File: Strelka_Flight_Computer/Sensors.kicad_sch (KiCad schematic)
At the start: 5 parts

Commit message: Started design for V2
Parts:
- added TP11, TP2, TP5: TestPoint, TestPoint:TestPoint_Pad_1.0x1.0mm, symbol Connector:TestPoint
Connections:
- net CS_ACCEL: now also TP2.1
- net CS_GYRO: now also TP5.1
- net CS_MAG: now also TP11.1
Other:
- note added: "Good Gyro Options - 511-I3G4250DTR - 410-IAM-20380 - ASM330LHHXTR"
- moved on the sheet: TP6, TP7, TP8

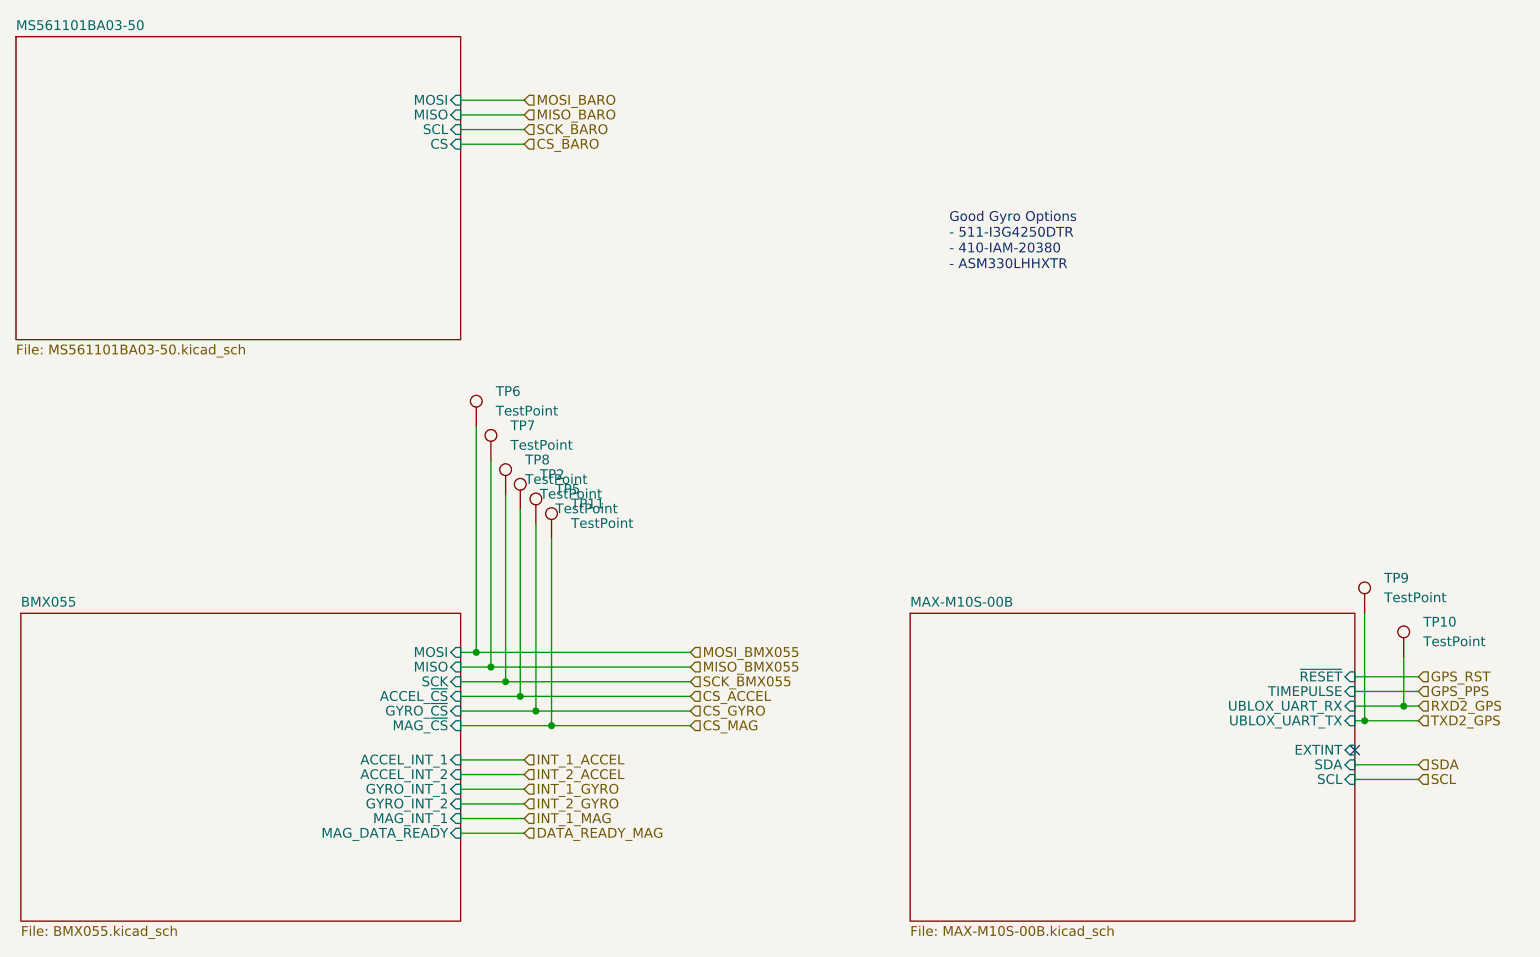
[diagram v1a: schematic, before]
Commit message: Changes main processor to h4745
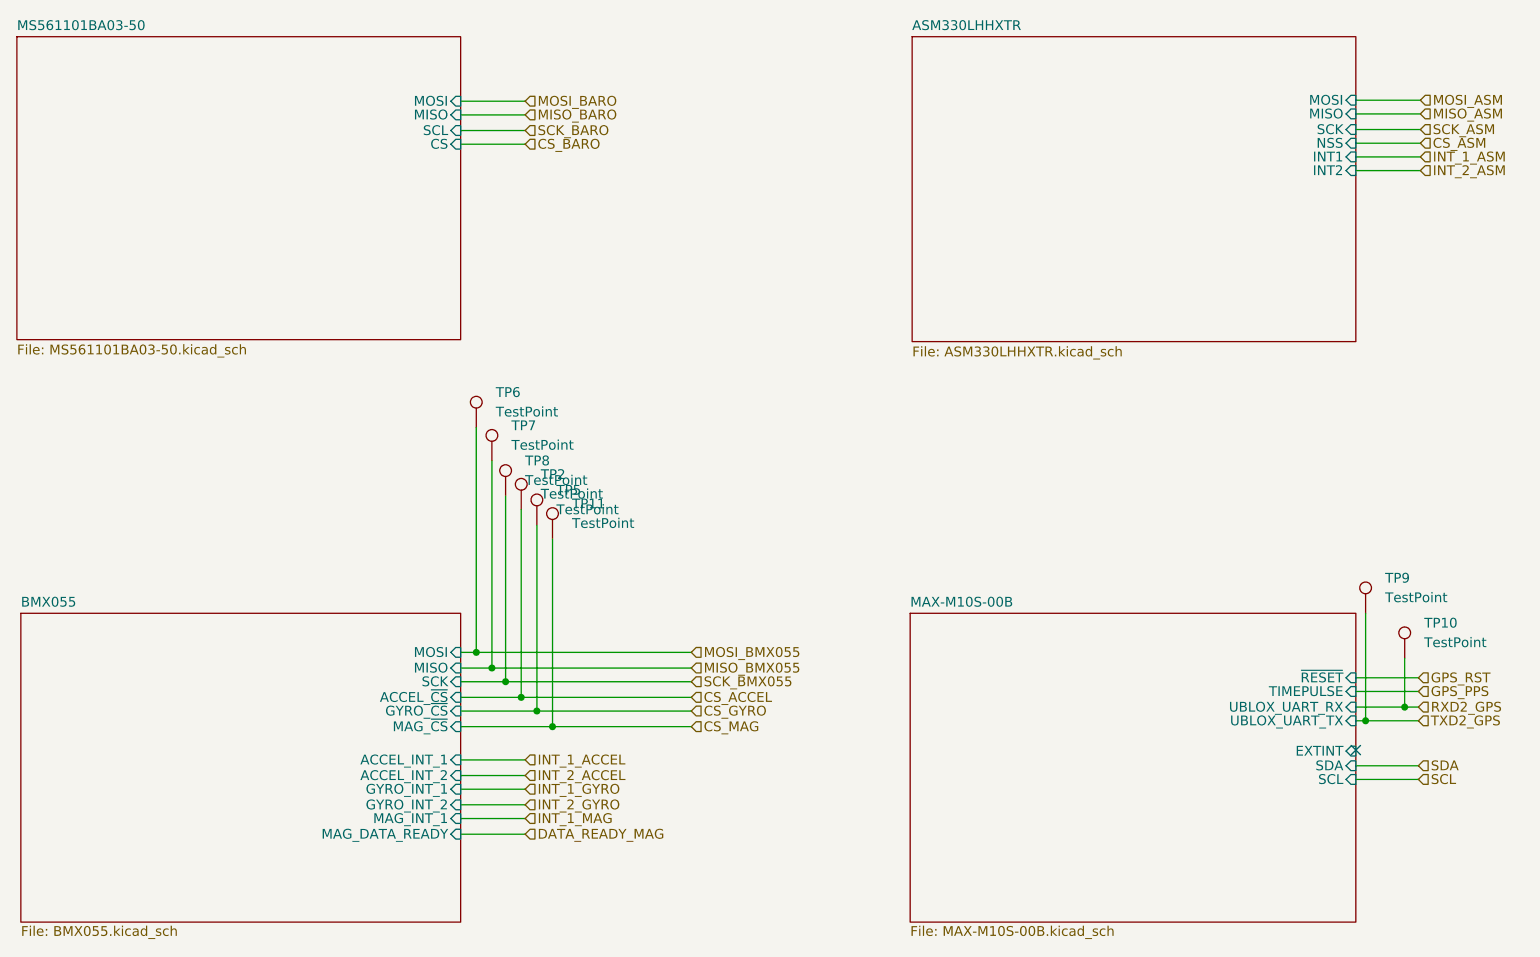
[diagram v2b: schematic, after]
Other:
- added sheet ASM330LHHXTR (ASM330LHHXTR.kicad_sch)
- note removed: "Good Gyro Options - 511-I3G4250DTR - 410-IAM-20380 - ASM330LHHXTR"

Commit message: Via stitched
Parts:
- removed TP11, TP2, TP5, TP6, TP7, TP8: TestPoint, TestPoint:TestPoint_Pad_1.0x1.0mm, symbol Connector:TestPoint
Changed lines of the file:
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@@
 (kicad_sch (version 20230121) (generator eeschema)
   (paper "A4")
-  (junction (at 107.188 122.682) (diameter 0) (color 0 0 0 0)
-  )
-  (junction (at 103.124 118.872) (diameter 0) (color 0 0 0 0)
-  )
   (junction (at 217.932 120.142) (diameter 0) (color 0 0 0 0)
   )
-  (junction (at 105.156 120.65) (diameter 0) (color 0 0 0 0)
-  )
-  (junction (at 101.092 116.84) (diameter 0) (color 0 0 0 0)
-  )
   (junction (at 212.852 121.92) (diameter 0) (color 0 0 0 0)
   )
-  (junction (at 97.282 113.03) (diameter 0) (color 0 0 0 0)
-  )
-  (junction (at 99.314 115.062) (diameter 0) (color 0 0 0 0)
-  )
   (no_connect (at 211.582 125.73))
-  (wire (pts (xy 107.188 98.298) (xy 107.188 122.682))
-    (stroke (width 0) (type default))
-  )
-  (wire (pts (xy 95.25 115.062) (xy 99.314 115.062))
-    (stroke (width 0) (type default))
-  )
-  (wire (pts (xy 105.156 120.65) (xy 125.222 120.65))
+  (wire (pts (xy 95.25 115.062) (xy 125.222 115.062))
     (stroke (width 0) (type default))
   )
@@
     (stroke (width 0) (type default))
   )
-  (wire (pts (xy 95.25 116.84) (xy 101.092 116.84))
+  (wire (pts (xy 95.25 116.84) (xy 125.222 116.84))
     (stroke (width 0) (type default))
   )
@@
     (stroke (width 0) (type default))
   )
-  (wire (pts (xy 105.156 96.52) (xy 105.156 120.65))
-    (stroke (width 0) (type default))
-  )
   (wire (pts (xy 217.932 113.792) (xy 217.932 120.142))
     (stroke (width 0) (type default))
   )
-  (wire (pts (xy 103.124 94.488) (xy 103.124 118.872))
-    (stroke (width 0) (type default))
-  )
-  (wire (pts (xy 97.282 83.82) (xy 97.282 113.03))
-    (stroke (width 0) (type default))
-  )
   (wire (pts (xy 95.25 45.212) (xy 103.632 45.212))
     (stroke (width 0) (type default))
@@
     (stroke (width 0) (type default))
   )
-  (wire (pts (xy 99.314 115.062) (xy 125.222 115.062))
-    (stroke (width 0) (type default))
-  )
-  (wire (pts (xy 107.188 122.682) (xy 125.222 122.682))
-    (stroke (width 0) (type default))
-  )
-  (wire (pts (xy 95.25 113.03) (xy 97.282 113.03))
-    (stroke (width 0) (type default))
-  )
-  (wire (pts (xy 97.282 113.03) (xy 125.222 113.03))
+  (wire (pts (xy 95.25 113.03) (xy 125.222 113.03))
     (stroke (width 0) (type default))
   )
@@
     (stroke (width 0) (type default))
   )
-  (wire (pts (xy 101.092 116.84) (xy 125.222 116.84))
-    (stroke (width 0) (type default))
-  )
   (wire (pts (xy 211.582 120.142) (xy 217.932 120.142))
     (stroke (width 0) (type default))
@@
     (stroke (width 0) (type default))
   )
-  (wire (pts (xy 99.314 88.138) (xy 99.314 115.062))
-    (stroke (width 0) (type default))
-  )
   (wire (pts (xy 211.582 48.641) (xy 219.964 48.641))
     (stroke (width 0) (type default))
@@
     (stroke (width 0) (type default))
   )
-  (wire (pts (xy 95.25 120.65) (xy 105.156 120.65))
-    (stroke (width 0) (type default))
-  )
-  (wire (pts (xy 95.25 122.682) (xy 107.188 122.682))
-    (stroke (width 0) (type default))
-  )
-  (wire (pts (xy 95.25 118.872) (xy 103.124 118.872))
+  (wire (pts (xy 95.25 120.65) (xy 125.222 120.65))
+    (stroke (width 0) (type default))
+  )
+  (wire (pts (xy 95.25 122.682) (xy 125.222 122.682))
+    (stroke (width 0) (type default))
+  )
+  (wire (pts (xy 95.25 118.872) (xy 125.222 118.872))
     (stroke (width 0) (type default))
   )
@@
   )
   (wire (pts (xy 211.582 118.11) (xy 219.71 118.11))
-    (stroke (width 0) (type default))
-  )
-  (wire (pts (xy 103.124 118.872) (xy 125.222 118.872))
-    (stroke (width 0) (type default))
-  )
-  (wire (pts (xy 101.092 92.71) (xy 101.092 116.84))
     (stroke (width 0) (type default))
   )
@@
         )
       )
-    )
-  )
-  (symbol (lib_id "Connector:TestPoint") (at 101.092 92.71 0) (unit 1)
-    (in_bom yes) (on_board yes) (dnp no) (fields_autoplaced)
-    (property "Reference" "TP8" (at 103.632 88.1379 0)
-      (effects (font (size 1.27 1.27)) (justify left))
-    )
-    (property "Value" "TestPoint" (at 103.632 90.6779 0)
-      (effects (font (size 1.27 1.27)) (justify left))
-    )
-    (property "Footprint" "TestPoint:TestPoint_Pad_1.0x1.0mm" (at 106.172 92.71 0)
-      (effects (font (size 1.27 1.27)) hide)
-    )
-    (property "Datasheet" "~" (at 106.172 92.71 0)
-      (effects (font (size 1.27 1.27)) hide)
-    )
-    (pin "1")
-    (instances
-      (project "Strelka_Flight_Computer"
-        (path "/e63e39d7-6ac0-4ffd-8aa3-1841a4541b55/78f71895-bddb-4f64-a608-99074f2d1c44"
-          (reference "TP8") (unit 1)
-        )
-      )
-    )
-  )
-  (symbol (lib_id "Connector:TestPoint") (at 107.188 98.298 0) (unit 1)
-    (in_bom yes) (on_board yes) (dnp no) (fields_autoplaced)
-    (property "Reference" "TP11" (at 109.728 93.7259 0)
-      (effects (font (size 1.27 1.27)) (justify left))
-    )
-    (property "Value" "TestPoint" (at 109.728 96.2659 0)
-      (effects (font (size 1.27 1.27)) (justify left))
-    )
-    (property "Footprint" "TestPoint:TestPoint_Pad_1.0x1.0mm" (at 112.268 98.298 0)
-      (effects (font (size 1.27 1.27)) hide)
-    )
-    (property "Datasheet" "~" (at 112.268 98.298 0)
-      (effects (font (size 1.27 1.27)) hide)
-    )
-    (pin "1")
-    (instances
-      (project "Strelka_Flight_Computer"
-        (path "/e63e39d7-6ac0-4ffd-8aa3-1841a4541b55/78f71895-bddb-4f64-a608-99074f2d1c44"
-          (reference "TP11") (unit 1)
-        )
-      )
-    )
-  )
-  (symbol (lib_id "Connector:TestPoint") (at 105.156 96.52 0) (unit 1)
-    (in_bom yes) (on_board yes) (dnp no) (fields_autoplaced)
-    (property "Reference" "TP5" (at 107.696 91.9479 0)
-      (effects (font (size 1.27 1.27)) (justify left))
-    )
-    (property "Value" "TestPoint" (at 107.696 94.4879 0)
-      (effects (font (size 1.27 1.27)) (justify left))
-    )
-    (property "Footprint" "TestPoint:TestPoint_Pad_1.0x1.0mm" (at 110.236 96.52 0)
-      (effects (font (size 1.27 1.27)) hide)
-    )
-    (property "Datasheet" "~" (at 110.236 96.52 0)
-      (effects (font (size 1.27 1.27)) hide)
-    )
-    (pin "1")
-    (instances
-      (project "Strelka_Flight_Computer"
-        (path "/e63e39d7-6ac0-4ffd-8aa3-1841a4541b55/78f71895-bddb-4f64-a608-99074f2d1c44"
-          (reference "TP5") (unit 1)
-        )
-      )
-    )
-  )
-  (symbol (lib_id "Connector:TestPoint") (at 99.314 88.138 0) (unit 1)
-    (in_bom yes) (on_board yes) (dnp no) (fields_autoplaced)
-    (property "Reference" "TP7" (at 101.854 83.5659 0)
-      (effects (font (size 1.27 1.27)) (justify left))
-    )
-    (property "Value" "TestPoint" (at 101.854 86.1059 0)
-      (effects (font (size 1.27 1.27)) (justify left))
-    )
-    (property "Footprint" "TestPoint:TestPoint_Pad_1.0x1.0mm" (at 104.394 88.138 0)
-      (effects (font (size 1.27 1.27)) hide)
-    )
-    (property "Datasheet" "~" (at 104.394 88.138 0)
-      (effects (font (size 1.27 1.27)) hide)
-    )
-    (pin "1")
-    (instances
-      (project "Strelka_Flight_Computer"
-        (path "/e63e39d7-6ac0-4ffd-8aa3-1841a4541b55/78f71895-bddb-4f64-a608-99074f2d1c44"
-          (reference "TP7") (unit 1)
-        )
-      )
-    )
-  )
-  (symbol (lib_id "Connector:TestPoint") (at 103.124 94.488 0) (unit 1)
-    (in_bom yes) (on_board yes) (dnp no) (fields_autoplaced)
-    (property "Reference" "TP2" (at 105.664 89.9159 0)
-      (effects (font (size 1.27 1.27)) (justify left))
-    )
-    (property "Value" "TestPoint" (at 105.664 92.4559 0)
-      (effects (font (size 1.27 1.27)) (justify left))
-    )
-    (property "Footprint" "TestPoint:TestPoint_Pad_1.0x1.0mm" (at 108.204 94.488 0)
-      (effects (font (size 1.27 1.27)) hide)
-    )
-    (property "Datasheet" "~" (at 108.204 94.488 0)
-      (effects (font (size 1.27 1.27)) hide)
-    )
-    (pin "1")
-    (instances
-      (project "Strelka_Flight_Computer"
-        (path "/e63e39d7-6ac0-4ffd-8aa3-1841a4541b55/78f71895-bddb-4f64-a608-99074f2d1c44"
-          (reference "TP2") (unit 1)
-        )
-      )
-    )
-  )
-  (symbol (lib_id "Connector:TestPoint") (at 97.282 83.82 0) (unit 1)
-    (in_bom yes) (on_board yes) (dnp no) (fields_autoplaced)
-    (property "Reference" "TP6" (at 99.822 79.2479 0)
-      (effects (font (size 1.27 1.27)) (justify left))
-    )
-    (property "Value" "TestPoint" (at 99.822 81.7879 0)
-      (effects (font (size 1.27 1.27)) (justify left))
-    )
-    (property "Footprint" "TestPoint:TestPoint_Pad_1.0x1.0mm" (at 102.362 83.82 0)
-      (effects (font (size 1.27 1.27)) hide)
-    )
-    (property "Datasheet" "~" (at 102.362 83.82 0)
-      (effects (font (size 1.27 1.27)) hide)
-    )
-    (pin "1")
-    (instances
-      (project "Strelka_Flight_Computer"
-        (path "/e63e39d7-6ac0-4ffd-8aa3-1841a4541b55/78f71895-bddb-4f64-a608-99074f2d1c44"
-          (reference "TP6") (unit 1)
-        )
-      )
